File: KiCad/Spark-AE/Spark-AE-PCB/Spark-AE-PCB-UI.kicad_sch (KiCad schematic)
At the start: 38 parts, among them Q1 2N3904, Q2 2N3904, SW1 SW_Push, SW2 SW_Push, U2 MCP6002-xSN, U3 Driver_LED_PCA9633PW,118

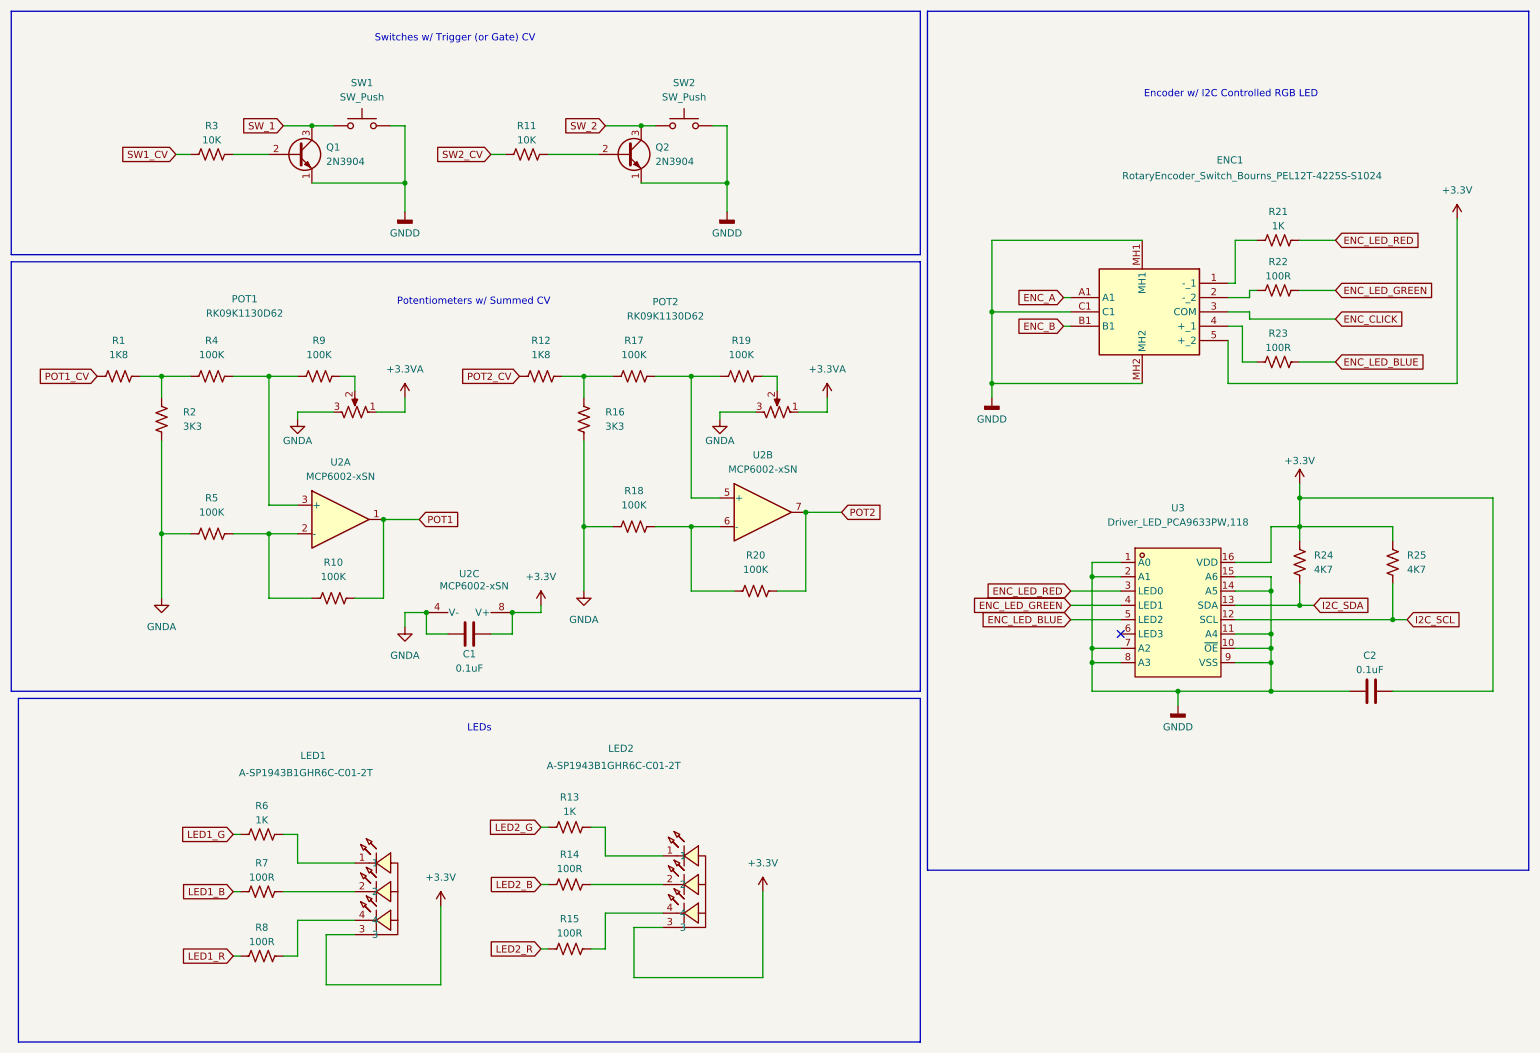
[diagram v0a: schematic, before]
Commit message: assigned footprints & sorted ratsnest
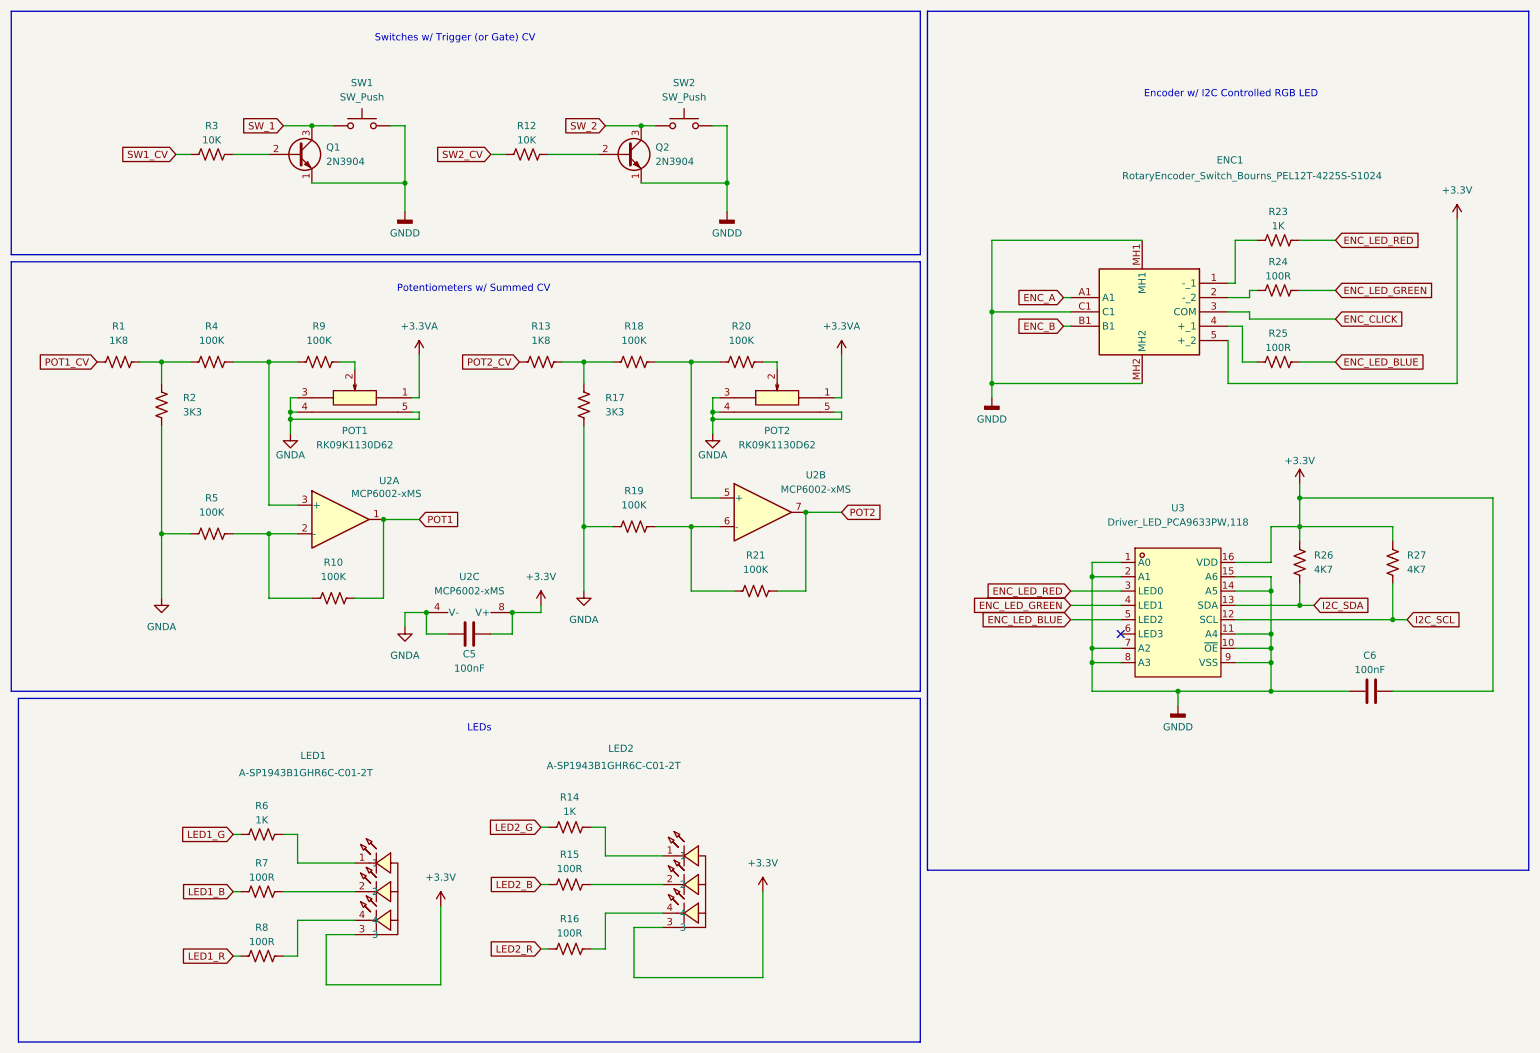
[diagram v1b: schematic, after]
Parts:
- removed POT1, POT2: RK09K1130D62, symbol Device:R_Potentiometer_US
- removed R19: 100K, symbol Device:R_US
- removed U2: MCP6002-xSN, symbol Amplifier_Operational:MCP6002-xSN
- added POT1, POT2: RK09K1130D62, clectric-diy:Potentiometer_THT_Alps_RK09K1130D62, symbol clectric-diy:R_Potentiometer_Alps_RK09K1130D62
- added R20: 100K, Resistor_SMD:R_0603_1608Metric, symbol Device:R_US
- added U2: MCP6002-xMS, clectric-diy:Amplifier_Operational_Microchip_MCP6002T-I_MS, symbol Amplifier_Operational:MCP6002-xMS
- C5: renamed from C1; value 0.1uF -> 100nF; footprint Capacitor_SMD:C_0805_2012Metric -> Capacitor_SMD:C_0603_1608Metric
- C6: renamed from C2; value 0.1uF -> 100nF; footprint Capacitor_SMD:C_0805_2012Metric -> Capacitor_SMD:C_0603_1608Metric
- LED1, LED2: footprint clectric-diy:LED-SMD_4P-L1.6-W1.5-BL_A-SP1943B1GHR6C-C01-2T -> clectric-diy:LED_ARGB_Amicc_A-SP1943B1GHR6C-C01-2T
- R1, R10, R2, R3, R4, R5, R6, R7, R8, R9: footprint (none) -> Resistor_SMD:R_0603_1608Metric
- R12: renamed from R11; footprint (none) -> Resistor_SMD:R_0603_1608Metric
- R13: renamed from R12; footprint (none) -> Resistor_SMD:R_0603_1608Metric
- R14: renamed from R13; footprint (none) -> Resistor_SMD:R_0603_1608Metric
- R15: renamed from R14; footprint (none) -> Resistor_SMD:R_0603_1608Metric
- R16: renamed from R15; footprint (none) -> Resistor_SMD:R_0603_1608Metric
- R17: renamed from R16; footprint (none) -> Resistor_SMD:R_0603_1608Metric
- R18: renamed from R17; footprint (none) -> Resistor_SMD:R_0603_1608Metric
- R19: renamed from R18; footprint (none) -> Resistor_SMD:R_0603_1608Metric
- R21: renamed from R20; footprint (none) -> Resistor_SMD:R_0603_1608Metric
- R23: renamed from R21; footprint (none) -> Resistor_SMD:R_0603_1608Metric
- R24: renamed from R22; footprint (none) -> Resistor_SMD:R_0603_1608Metric
- R25: renamed from R23; footprint (none) -> Resistor_SMD:R_0603_1608Metric
- R26: renamed from R24; footprint (none) -> Resistor_SMD:R_0603_1608Metric
- R27: renamed from R25; footprint (none) -> Resistor_SMD:R_0603_1608Metric
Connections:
- net +3.3V: now also U2.8 (V+)
- net +3.3VA: now also POT1.1, POT2.1
- net GNDA: now also POT1.3, POT1.4 (EH), POT1.5 (EH), POT2.3, POT2.4 (EH), POT2.5 (EH), U2.4 (V-)
- net POT1: now also U2.1
- net POT2: now also U2.7
- net at R18.2: now also R20.1, U2.5 (+)
- net at R19.2, R21.1: now also U2.6 (-)
- net at R10.1, R5.2: now also U2.2 (-)
- net at R4.2, R9.1: now also U2.3 (+)
- net at R9.2: now also POT1.2
- new net: POT2.2, R20.2
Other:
- moved on the sheet: R1, R13, R17, R18, R2, R4, R9

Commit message: schematic 100% complete. pcb layout around 50% complete.
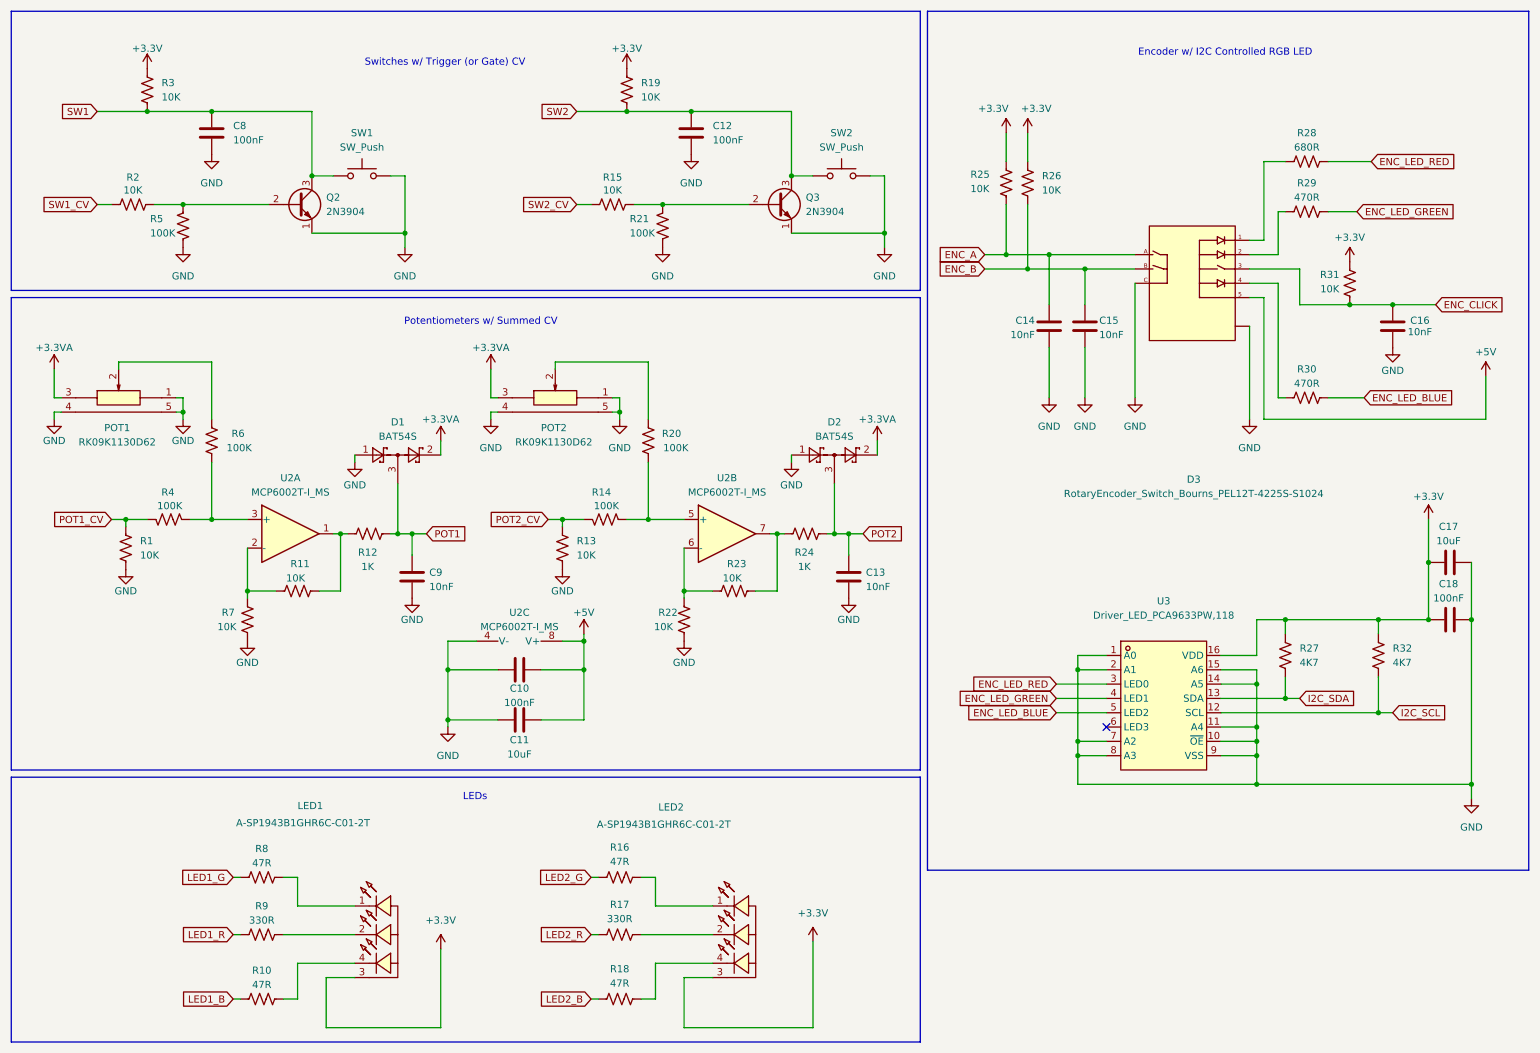
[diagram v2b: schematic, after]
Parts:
- removed ENC1: RotaryEncoder_Switch_Bourns_PEL12T-4225S-S1024, clectric-diy:RotaryEncoder_Switch_Bourns_PEL12T-4225S-S1024, symbol clectric-diy:RotaryEncoder_Switch_Bourns_PEL12T-4225S-S1024
- removed Q2: 2N3904, Package_TO_SOT_THT:TO-92_Inline, symbol Transistor_BJT:2N3904
- removed R10, R18, R9: 100K, Resistor_SMD:R_0603_1608Metric, symbol Device:R_US
- removed R17, R2: 3K3, Resistor_SMD:R_0603_1608Metric, symbol Device:R_US
- added C11, C17: 10uF, Capacitor_SMD:C_0603_1608Metric, symbol Device:C
- added C12, C8: 100nF, Capacitor_SMD:C_0603_1608Metric, symbol Device:C
- added C13, C14, C15, C16, C9: 10nF, Capacitor_SMD:C_0603_1608Metric, symbol Device:C
- added D1, D2: BAT54S, Package_TO_SOT_SMD:SOT-23, symbol Diode:BAT54S
- added D3: RotaryEncoder_Switch_Bourns_PEL12T-4225S-S1024, clectric-diy:RotaryEncoder_Switch_Bourns_PEL12T-4225S-S1024, symbol clectric-diy:RotaryEncoder_Switch_Bourns_PEL12T-4225S-S1024
- added Q3: 2N3904, Package_TO_SOT_THT:TO-92_Inline, symbol Transistor_BJT:2N3904
- added R11, R15, R22, R23, R25, R26, R3, R31, R7: 10K, Resistor_SMD:R_0603_1608Metric, symbol Device:R_US
- added R14, R6: 100K, Resistor_SMD:R_0603_1608Metric, symbol Device:R_US
- added R24: 1K, Resistor_SMD:R_0603_1608Metric, symbol Device:R_US
- R1, R13: value 1K8 -> 10K
- R10: renamed from R8; value 100R -> 47R
- R12: value 10K -> 1K
- R16: renamed from R14; value 1K -> 47R
- R17: renamed from R15; value 100R -> 330R
- R18: renamed from R16; value 100R -> 47R
- R19: value 100K -> 10K
- R28: renamed from R23; value 1K -> 680R
- R29: renamed from R24; value 100R -> 470R
- R30: renamed from R25; value 100R -> 470R
- R8: renamed from R6; value 1K -> 47R
- R9: renamed from R7; value 100R -> 330R
- U2: value MCP6002-xMS -> MCP6002T-I_MS
- renumbered C5 to C10, C6 to C18, Q1 to Q2, R3 to R2, R26 to R27, R27 to R32
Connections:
- net +3.3V: now also C18.1, R19.1, C17.1, R25.1, R26.1, R3.1, R31.1; no longer C10.2, C18.2, U2.8 (V+)
- net +3.3VA: now also POT1.3, POT2.3, D1.2 (K), D2.2 (K); no longer POT1.1, POT2.1
- net ENC_A: now also C14.1, D3.A, R25.2
- net ENC_B: now also C15.1, D3.B, R26.2
- net ENC_CLICK: now also C16.2, D3.3, R31.2
- net LED1_B: now also R10.1; no longer R9.1
- net LED1_R: now also R9.1; no longer R10.1
- net LED2_B: now also R18.1; no longer R17.1
- net LED2_R: now also R17.1; no longer R18.1
- net POT1: now also R12.2, C9.1, D1.3 (COM); no longer U2.1
- net POT1_CV: now also R4.2
- net POT2: now also C13.1, D2.3 (COM), R24.2; no longer R21.2, U2.7
- net POT2_CV: now also R14.2
- net SW2_CV: now also R15.1; no longer R12.1
- net at R29.1: now also D3.2
- net at U2.2 (-): now also R11.1, R7.1; no longer R5.2
- net at U2.3 (+): now also R4.1, R6.2; no longer R4.2
- net GND: now reaches R13.2
- net GND: now also C10.2, C18.2, POT1.1, POT1.4 (EH), POT1.5 (EH), POT2.1, POT2.4 (EH), POT2.5 (EH), Q2.1 (E), R1.2, R21.2, R5.2, SW1.2, SW2.2, U2.4 (V-), U3.1 (A0), U3.10 (~{OE}), U3.11 (A4), U3.14 (A5), U3.15 (A6), U3.2 (A1), U3.7 (A2), U3.8 (A3), U3.9 (VSS), C11.1, C12.2, C13.2, C14.2, C15.2, C16.1, C17.2, C8.2, C9.2, D1.1 (A), D2.1 (A), D3.C, D3.S1 (SHIELD), D3.S2 (SHIELD__1), Q3.1 (E), R22.2, R7.2
- net at R28.1: now also D3.1
- net at POT1.2: now also R6.1
- net at R20.2: now also U2.5 (+), R14.1; no longer POT2.2
- net at Q2.2 (B), R2.2: now also R5.1
- net at R30.1: now also D3.4
- net at R20.1: now also POT2.2; no longer U2.5 (+)
- removed net GNDA: C10.1, POT1.3, POT1.4 (EH), POT1.5 (EH), POT2.3, POT2.4 (EH), POT2.5 (EH), R19.1, R5.1, U2.4 (V-)
- removed net GNDD: C18.1, Q2.1 (E), SW1.2, SW2.2, U3.1 (A0), U3.10 (~{OE}), U3.11 (A4), U3.14 (A5), U3.15 (A6), U3.2 (A1), U3.7 (A2), U3.8 (A3), U3.9 (VSS)
- net SW_1 renamed SW1
- net SW1: now also C8.1, R3.2
- net SW_2 renamed SW2
- net SW2: now also R19.2, C12.1, Q3.3 (C)
- new net: R22.1, R23.1, U2.6 (-)
- new net: R11.2, R12.1, U2.1
- new net: R23.2, R24.1, U2.7
- new net: Q3.2 (B), R15.2, R21.1
- new net +5V: C10.1, C11.2, D3.5, U2.8 (V+)
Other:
- moved on the sheet: C10, C18, POT1, Q2, R10, R16, R17, R18, R2, R27, R28, R29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

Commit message: continuing to plug away at pcb layout
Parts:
- renumbered C12 to C10, C13 to C11, C14 to C12, C15 to C13, C16 to C14, C17 to C15, C18 to C16, C8 to C6, C9 to C7, C10 to C8, C11 to C9
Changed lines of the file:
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@@
 		(on_board yes)
 		(dnp no)
-		(property "Reference" "C9"
+		(property "Reference" "C7"
 			(at 88.138 112.268 0)
 			(effects
@@
 			(project ""
 				(path "/b249adcd-2848-4e56-9615-c4f1b6083abe/07992dbf-5cfc-457b-89f1-5f6a46dfeac6"
-					(reference "C9")
+					(reference "C7")
 					(unit 1)
 				)
@@
 		(on_board yes)
 		(dnp no)
-		(property "Reference" "C14"
+		(property "Reference" "C12"
 			(at 195.58 67.564 0)
 			(effects
@@
 			(project "Spark-AE-PCB"
 				(path "/b249adcd-2848-4e56-9615-c4f1b6083abe/07992dbf-5cfc-457b-89f1-5f6a46dfeac6"
-					(reference "C14")
+					(reference "C12")
 					(unit 1)
 				)
@@
 		(on_board yes)
 		(dnp no)
-		(property "Reference" "C17"
+		(property "Reference" "C15"
 			(at 268.986 104.14 90)
 			(effects
@@
 			(project "Spark-AE-PCB"
 				(path "/b249adcd-2848-4e56-9615-c4f1b6083abe/07992dbf-5cfc-457b-89f1-5f6a46dfeac6"
-					(reference "C17")
+					(reference "C15")
 					(unit 1)
 				)
@@
 		(on_board yes)
 		(dnp no)
-		(property "Reference" "C16"
+		(property "Reference" "C14"
 			(at 263.906 67.564 0)
 			(effects
@@
 			(project "Spark-AE-PCB"
 				(path "/b249adcd-2848-4e56-9615-c4f1b6083abe/07992dbf-5cfc-457b-89f1-5f6a46dfeac6"
-					(reference "C16")
+					(reference "C14")
 					(unit 1)
 				)
@@
 		(on_board yes)
 		(dnp no)
-		(property "Reference" "C11"
+		(property "Reference" "C9"
 			(at 104.14 141.986 90)
 			(effects
@@
 			(project "Spark-AE-PCB"
 				(path "/b249adcd-2848-4e56-9615-c4f1b6083abe/07992dbf-5cfc-457b-89f1-5f6a46dfeac6"
-					(reference "C11")
+					(reference "C9")
 					(unit 1)
 				)
@@
 		(dnp no)
 		(fields_autoplaced yes)
-		(property "Reference" "C12"
+		(property "Reference" "C10"
 			(at 138.43 33.0199 0)
 			(effects
@@
 			(project "Spark-AE-PCB"
 				(path "/b249adcd-2848-4e56-9615-c4f1b6083abe/07992dbf-5cfc-457b-89f1-5f6a46dfeac6"
-					(reference "C12")
+					(reference "C10")
 					(unit 1)
 				)
@@
 		(on_board yes)
 		(dnp no)
-		(property "Reference" "C13"
+		(property "Reference" "C11"
 			(at 165.608 112.268 0)
 			(effects
@@
 			(project "Spark-AE-PCB"
 				(path "/b249adcd-2848-4e56-9615-c4f1b6083abe/07992dbf-5cfc-457b-89f1-5f6a46dfeac6"
-					(reference "C13")
+					(reference "C11")
 					(unit 1)
 				)
@@
 		(lib_id "Device:R_US")
 		(at 127 88.9 0)
+		(mirror y)
 		(unit 1)
 		(exclude_from_sim no)
@@
 		(dnp no)
 		(property "Reference" "R20"
-			(at 132.842 87.63 0)
+			(at 121.158 87.63 0)
 			(effects
 				(font
@@
 		)
 		(property "Value" "100K"
-			(at 134.112 90.17 0)
+			(at 119.888 90.17 0)
 			(effects
 				(font
@@
 		)
 		(property "Footprint" "Resistor_SMD:R_0603_1608Metric"
-			(at 128.016 89.154 90)
+			(at 125.984 89.154 90)
 			(effects
 				(font
@@
 		(on_board yes)
 		(dnp no)
-		(property "Reference" "C10"
+		(property "Reference" "C8"
 			(at 104.14 132.842 90)
 			(effects
@@
 			(project "Spark-AE-PCB"
 				(path "/b249adcd-2848-4e56-9615-c4f1b6083abe/07992dbf-5cfc-457b-89f1-5f6a46dfeac6"
-					(reference "C10")
+					(reference "C8")
 					(unit 1)
 				)
@@
 		(on_board yes)
 		(dnp no)
-		(property "Reference" "C18"
+		(property "Reference" "C16"
 			(at 268.986 114.3 90)
 			(effects
@@
 			(project "Spark-AE-PCB"
 				(path "/b249adcd-2848-4e56-9615-c4f1b6083abe/07992dbf-5cfc-457b-89f1-5f6a46dfeac6"
-					(reference "C18")
+					(reference "C16")
 					(unit 1)
 				)
@@
 		(dnp no)
 		(fields_autoplaced yes)
-		(property "Reference" "C8"
+		(property "Reference" "C6"
 			(at 53.34 33.0199 0)
 			(effects
@@
 			(project ""
 				(path "/b249adcd-2848-4e56-9615-c4f1b6083abe/07992dbf-5cfc-457b-89f1-5f6a46dfeac6"
-					(reference "C8")
+					(reference "C6")
 					(unit 1)
 				)
@@
 		(on_board yes)
 		(dnp no)
-		(property "Reference" "C15"
+		(property "Reference" "C13"
 			(at 207.01 67.564 0)
 			(effects
@@
 			(project ""
 				(path "/b249adcd-2848-4e56-9615-c4f1b6083abe/07992dbf-5cfc-457b-89f1-5f6a46dfeac6"
-					(reference "C15")
+					(reference "C13")
 					(unit 1)
 				)

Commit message: I accdently upgraded to KiCad 10 via a `brew upgrade`. I committing before launching it just in case.
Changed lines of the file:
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@@
 		(on_board yes)
 		(dnp no)
-		(fields_autoplaced yes)
 		(property "Reference" "SW1"
 			(at 76.2 34.29 0)
@@
 		(lib_id "Device:C")
 		(at 162.56 113.03 0)
+		(mirror y)
 		(unit 1)
 		(exclude_from_sim no)
@@
 		(dnp no)
 		(property "Reference" "C11"
-			(at 165.608 112.268 0)
+			(at 159.512 112.268 0)
 			(effects
 				(font
@@
 		)
 		(property "Value" "10nF"
-			(at 165.608 114.808 0)
+			(at 159.512 114.808 0)
 			(effects
 				(font
@@
 		)
 		(property "Footprint" "Capacitor_SMD:C_0603_1608Metric"
-			(at 163.5252 116.84 0)
-			(effects
-				(font
+			(at 161.5948 116.84 0)
+			(effects
+				(font
